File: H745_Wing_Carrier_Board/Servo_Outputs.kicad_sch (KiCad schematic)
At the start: 4 parts

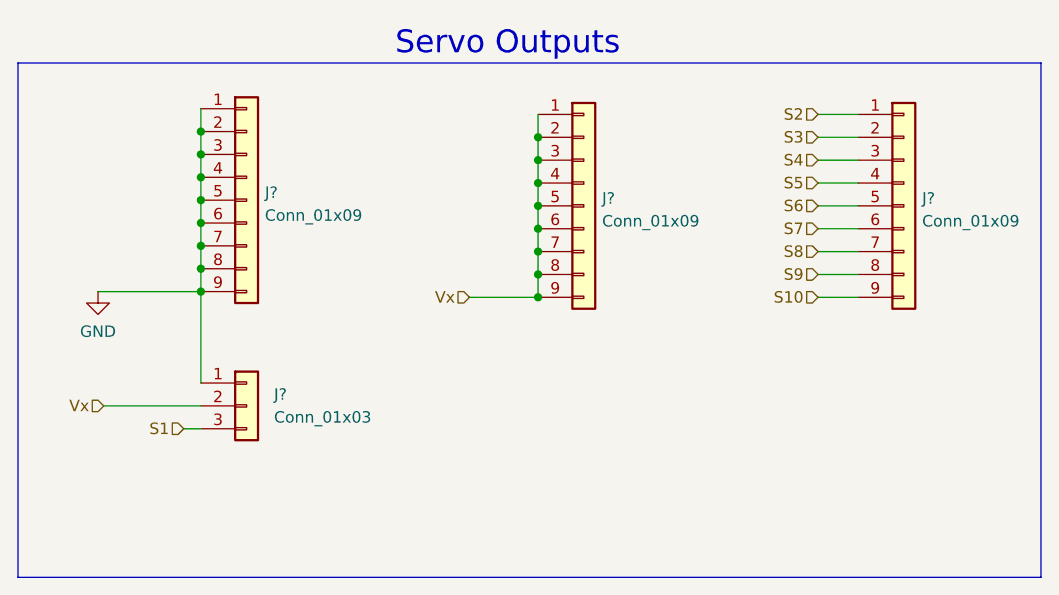
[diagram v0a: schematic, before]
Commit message: Added footprints for ux
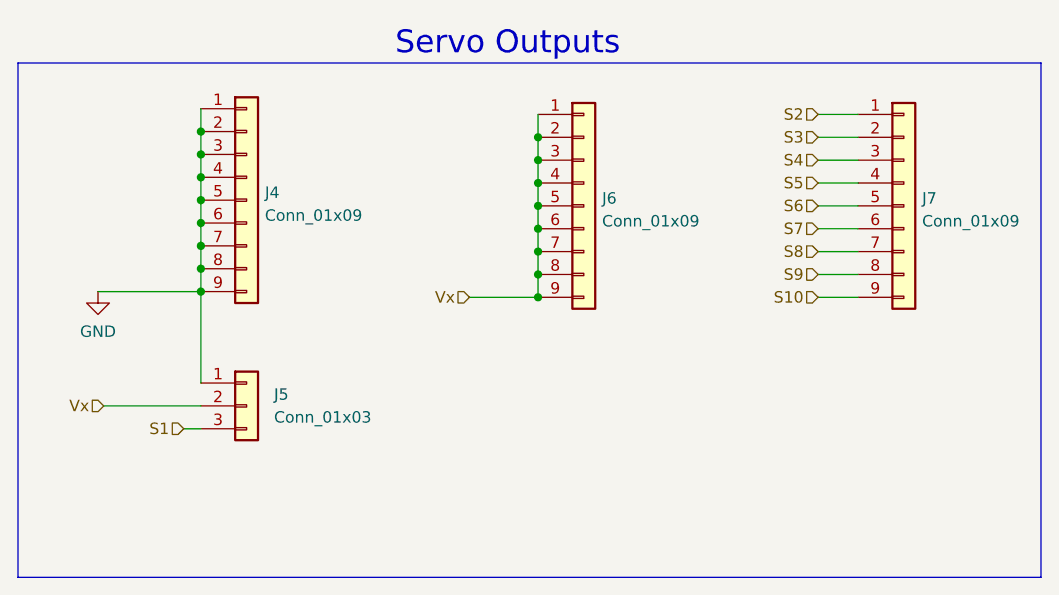
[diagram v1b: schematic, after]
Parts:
- gave numbers to parts that had none: 4
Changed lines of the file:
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@@
   (symbol (lib_id "Connector_Generic:Conn_01x03") (at 116.84 104.775 0) (unit 1)
     (in_bom yes) (on_board yes) (fields_autoplaced)
-    (property "Reference" "J?" (id 0) (at 119.888 103.5049 0)
+    (property "Reference" "J5" (id 0) (at 119.888 103.5049 0)
       (effects (font (size 1.27 1.27)) (justify left))
     )
@@
   (symbol (lib_id "Connector_Generic:Conn_01x09") (at 116.84 81.915 0) (unit 1)
     (in_bom yes) (on_board yes) (fields_autoplaced)
-    (property "Reference" "J?" (id 0) (at 118.872 81.0803 0)
+    (property "Reference" "J4" (id 0) (at 118.872 81.0803 0)
       (effects (font (size 1.27 1.27)) (justify left))
     )
@@
   (symbol (lib_id "power:GND") (at 100.33 92.075 0) (unit 1)
     (in_bom yes) (on_board yes) (fields_autoplaced)
-    (property "Reference" "#PWR?" (id 0) (at 100.33 98.425 0)
+    (property "Reference" "#PWR0106" (id 0) (at 100.33 98.425 0)
       (effects (font (size 1.27 1.27)) hide)
     )
@@
   (symbol (lib_id "Connector_Generic:Conn_01x09") (at 189.865 82.55 0) (unit 1)
     (in_bom yes) (on_board yes) (fields_autoplaced)
-    (property "Reference" "J?" (id 0) (at 191.897 81.7153 0)
+    (property "Reference" "J7" (id 0) (at 191.897 81.7153 0)
       (effects (font (size 1.27 1.27)) (justify left))
     )
@@
   (symbol (lib_id "Connector_Generic:Conn_01x09") (at 154.305 82.55 0) (unit 1)
     (in_bom yes) (on_board yes) (fields_autoplaced)
-    (property "Reference" "J?" (id 0) (at 156.337 81.7153 0)
+    (property "Reference" "J6" (id 0) (at 156.337 81.7153 0)
       (effects (font (size 1.27 1.27)) (justify left))
     )
